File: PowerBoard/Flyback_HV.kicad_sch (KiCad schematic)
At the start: 62 parts, among them Q2 FDD86250-F085, Q3 FGH50T65SQD-F155, Q5 TN2130K1-G, Q6 STD11N60DM2, Q7 FGH50T65SQD-F155, T1 750032050, U2 LT3750, U4 MCP14A0454-E/SN

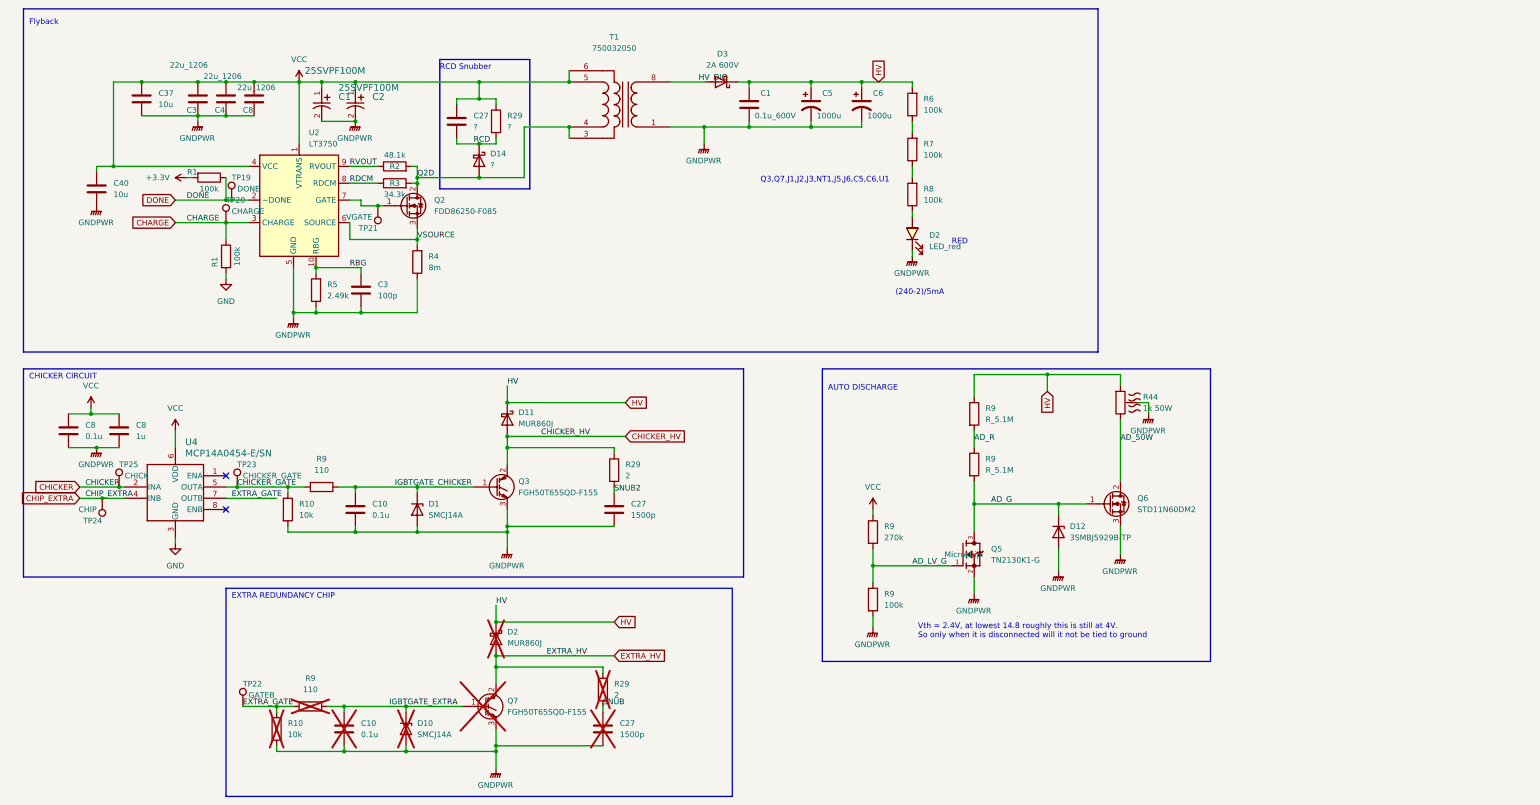
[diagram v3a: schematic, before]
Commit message: power board and midplate updates (mostly finalized)
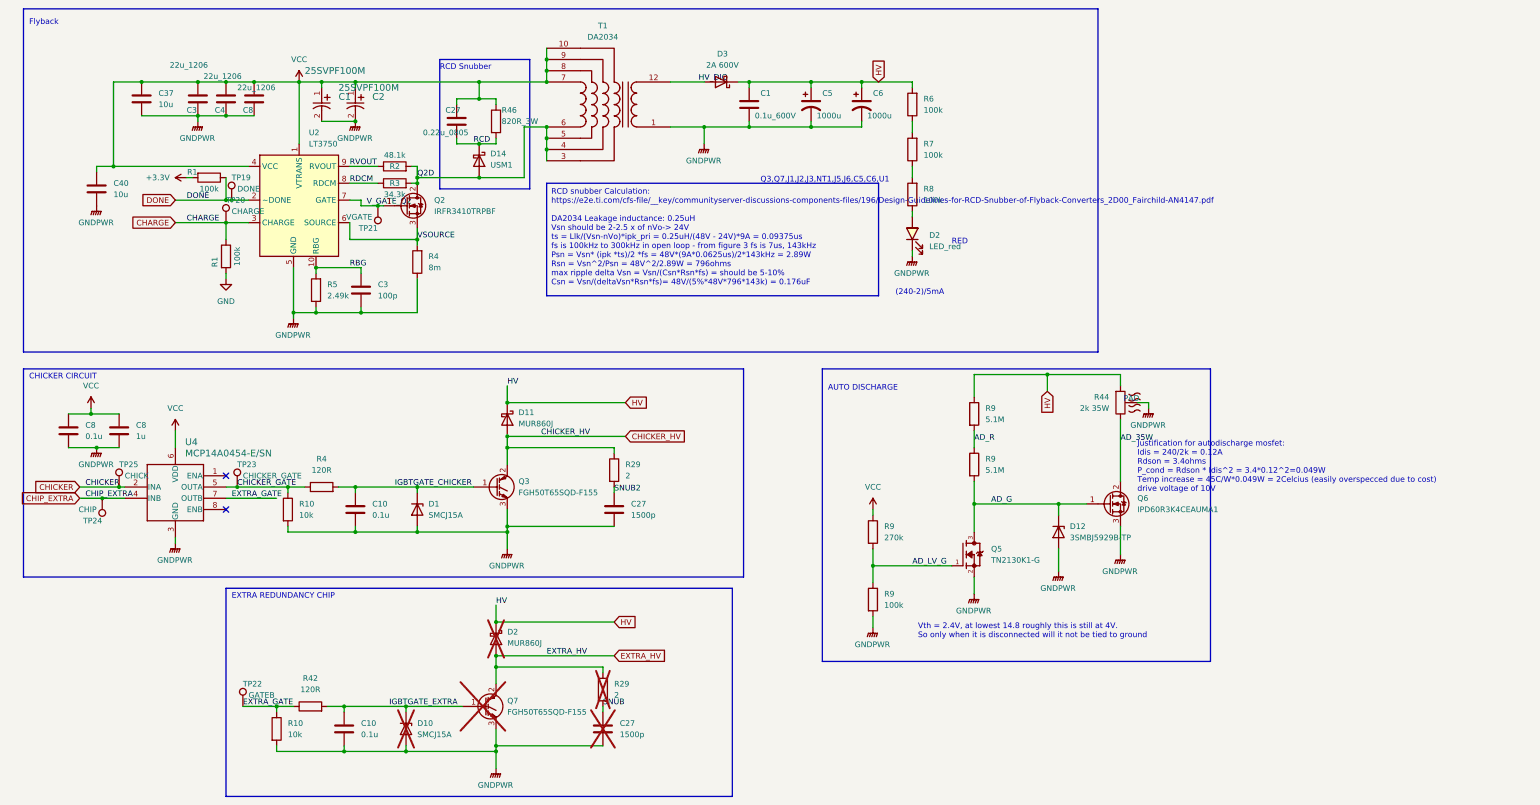
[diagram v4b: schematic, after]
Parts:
- removed C27: ?, bots:C_0805_2012Metric, symbol bots:C_1500p
- removed D1, D10: SMCJ14A, bots:D_SMC, symbol bots:SMCJ14A
- removed D14: ?, bots:D_SMA, symbol bots:MURS160-E3/52T
- removed Q2: FDD86250-F085, bots:DPAK-3_ONS, symbol bots:FDD86250-F085
- removed Q6: STD11N60DM2, bots:DPAK-3_ONS, symbol bots:STD11N60DM2
- removed R29: ?, bots:R_0805_2012Metric, symbol bots:R_2R_0805
- removed R44: 1k 50W, bots:TO-263-2, symbol bots:1k 50W
- removed R9 (x2): 110, bots:R_0603_1608Metric, symbol bots:R_110R
- removed T1: 750032050, bots:SMT_32050_WRE, symbol bots:Wurth_750032050
- added C27: 0.22u_0805, bots:C_0805_2012Metric, symbol bots:C_0.22u_0805
- added D1, D10: SMCJ15A, bots:D_SMC, symbol bots:SMCJ15A
- added D14: USM1, bots:D_SMA, symbol bots:D_USM1
- added Q2: IRFR3410TRPBF, bots:DPAK-3_ONS, symbol bots:IRFR3410TRPBF
- added Q6: IPD60R3K4CEAUMA1, bots:DPAK-3_ONS, symbol bots:IPD60R3K4CEAUMA1
- added R4, R42: 120R, bots:R_0603_1608Metric, symbol bots:R_120R
- added R44: 2k 35W, bots:TO-220-2_Horizontal_TabDown, symbol bots:2k_35W
- added R46: 820R_3W, bots:R_2512_6332Metric, symbol bots:R_820R_3W
- added T1: DA2034, bots:DA2034-ALD_COC, symbol bots:DA2034
- C10: now fitted; now in the parts list
- C27, D2, Q7, R29: now left out of the parts list
- D12: LCSC (none) -> N/A
- D2: footprint bots:LED_1206_3216Metric -> bots:LED_1206MERGE0805; JLC SMD,1.5x3.2mm -> 0805; JLC Extended (none) -> no; LCSC C2908310 -> C84256; MPN RF-RUT112TS-BD -> NCD0805R1; Manufacturer Refond -> Foshan NationStar Optoelectronics; Price 0.1023 -> 0.0122
- Q5: JLC Extended (none) -> yes; MF (none) -> Diodes Inc.; Price 0.67 -> 0.65
- R10: JLC Extended (none) -> no; now fitted; now in the parts list
- R10, R9: JLC Extended (none) -> no
- R9: value R_5.1M -> 5.1M; JLC Extended yes -> no; LCSC C322178 -> C13320; MPN RS-03L5104FT -> 0603WAF5104T5E; Manufacturer FH (Guangdong Fenghua Advanced Tech) -> UNI-ROYAL(Uniroyal Elec)
- R9: value R_5.1M -> 5.1M; JLC Extended (none) -> no; LCSC C322178 -> C13320; MPN RS-03L5104FT -> 0603WAF5104T5E; Manufacturer FH (Guangdong Fenghua Advanced Tech) -> UNI-ROYAL(Uniroyal Elec)
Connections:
- net AD_G: now also Q6.1 (G)
- net CHICKER_GATE: now also R4.1
- net EXTRA_GATE: now also R42.1
- net GND: no longer U4.3 (GND)
- net GNDPWR: now also U4.3 (GND), D1.2 (A), D10.2 (A), Q6.3 (S), R44.3 (PAD), T1.1 (SB)
- net HV: now also R44.1
- net HV_DIO: now also T1.12 (SB)
- net IGBTGATE_CHICKER: now also D1.1 (K), R4.2
- net IGBTGATE_EXTRA: now also D10.1 (K), R42.2
- net Q2D: now also D14.2 (A), Q2.2 (D), T1.3 (AB), T1.4 (AB), T1.5 (AB), T1.6 (AA)
- net RCD: now also C27.2, D14.1 (K), R46.2
- net VCC: now also C27.1, R46.1, T1.10 (AA), T1.7 (AA), T1.8 (AA), T1.9 (AA)
- net VSOURCE: now also Q2.3 (S)
- net V_GATE_Q2: now reaches TP21.1, U2.7 (GATE)
- net V_GATE_Q2: now also Q2.1 (G)
- new net AD_35W: Q6.2 (D), R44.2
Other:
- note added: "Justification for autodischarge mosfet: Idis = 240/2k = 0.12A Rdson = 3.4ohms P_cond = Rdson * Idis^2 = 3.4*0.12^2=0.049W Temp increase = 45C/W*0.049W = 2Celcius (easily overspecced due to cost) drive voltage of 10V"

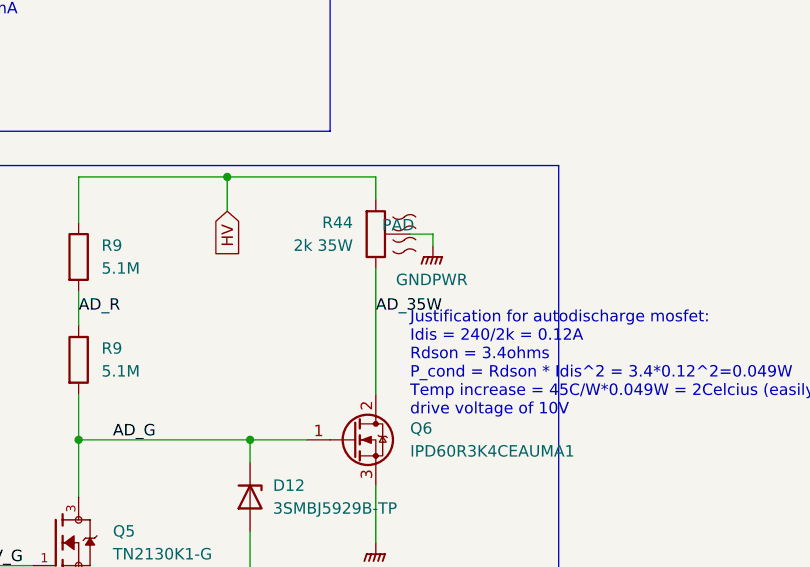
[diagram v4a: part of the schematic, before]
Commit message: discharge circuit changes
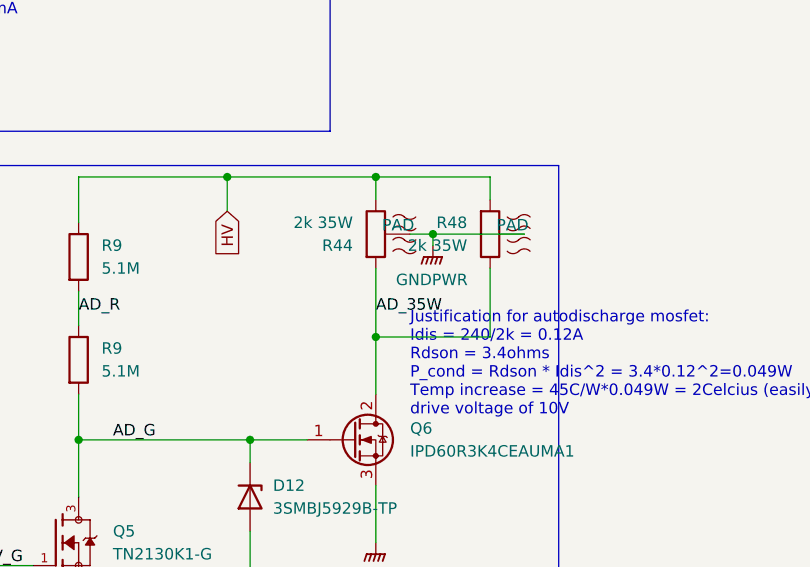
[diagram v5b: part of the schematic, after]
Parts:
- added R48: 2k 35W, bots:TO-220-2_Horizontal_TabDown, symbol bots:2k_35W
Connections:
- net AD_35W: now also R44.1, R48.2; no longer R44.2
- net GNDPWR: now also R48.3 (PAD)
- net HV: now also R44.2, R48.1; no longer R44.1
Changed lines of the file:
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@@
   (junction (at 104.14 53.34) (diameter 0) (color 0 0 0 0)
   )
+  (junction (at 262.89 97.79) (diameter 0) (color 0 0 0 0)
+  )
+  (junction (at 262.89 115.57) (diameter 0) (color 0 0 0 0)
+  )
   (junction (at 60.96 39.37) (diameter 0) (color 0 0 0 0)
   )
@@
   (junction (at 118.11 53.34) (diameter 0) (color 0 0 0 0)
   )
+  (junction (at 269.24 104.14) (diameter 0) (color 0 0 0 0)
+  )
   (junction (at 91.44 83.82) (diameter 0) (color 0 0 0 0)
   )
@@
     (stroke (width 0) (type default))
   )
+  (wire (pts (xy 275.59 115.57) (xy 262.89 115.57))
+    (stroke (width 0) (type default))
+  )
   (wire (pts (xy 113.03 35.56) (xy 118.11 35.56))
     (stroke (width 0) (type default))
@@
     (stroke (width 0) (type default))
   )
+  (wire (pts (xy 275.59 97.79) (xy 262.89 97.79))
+    (stroke (width 0) (type default))
+  )
   (wire (pts (xy 121.92 149.86) (xy 121.92 153.67))
     (stroke (width 0) (type default))
@@
     (stroke (width 0) (type default))
   )
+  (wire (pts (xy 275.59 107.95) (xy 275.59 115.57))
+    (stroke (width 0) (type default))
+  )
   (wire (pts (xy 113.03 36.83) (xy 113.03 35.56))
     (stroke (width 0) (type default))
@@
     (stroke (width 0) (type default))
   )
+  (wire (pts (xy 275.59 100.33) (xy 275.59 97.79))
+    (stroke (width 0) (type default))
+  )
   (wire (pts (xy 91.44 59.69) (xy 91.44 58.42))
     (stroke (width 0) (type default))
@@
     (stroke (width 0) (type default))
   )
+  (wire (pts (xy 269.24 104.14) (xy 279.4 104.14))
+    (stroke (width 0) (type default))
+  )
   (wire (pts (xy 179.07 31.75) (xy 193.04 31.75))
     (stroke (width 0) (type default))
@@
     (stroke (width 0) (type default))
   )
-  (wire (pts (xy 262.89 107.95) (xy 262.89 121.92))
+  (wire (pts (xy 262.89 107.95) (xy 262.89 115.57))
     (stroke (width 0) (type default))
   )
@@
     (stroke (width 0) (type default))
   )
+  (wire (pts (xy 262.89 115.57) (xy 262.89 121.92))
+    (stroke (width 0) (type default))
+  )
   (wire (pts (xy 25.4 106.68) (xy 30.48 106.68))
     (stroke (width 0) (type default))
@@
     )
   )
-  (symbol (lib_id "bots:2k_35W") (at 262.89 104.14 0) (unit 1)
-    (in_bom yes) (on_board yes) (dnp no) (fields_autoplaced)
-    (property "Reference" "R44" (at 260.35 102.87 0)
-      (effects (font (size 1.27 1.27)) (justify right))
-    )
-    (property "Value" "2k 35W" (at 260.35 105.41 0)
-      (effects (font (size 1.27 1.27)) (justify right))
-    )
-    (property "Footprint" "bots:TO-220-2_Horizontal_TabDown" (at 261.112 104.14 90)
-      (effects (font (size 1.27 1.27)) hide)
-    )
-    (property "Datasheet" "~" (at 262.89 104.14 0)
-      (effects (font (size 1.27 1.27)) hide)
-    )
-    (property "MPN" "PWR220T-35-2001J" (at 262.89 104.14 0)
-      (effects (font (size 1.27 1.27)) hide)
-    )
-    (property "Manufacturer" "Bourns" (at 262.89 104.14 0)
-      (effects (font (size 1.27 1.27)) hide)
-    )
-    (property "Price" "4.067" (at 262.89 104.14 0)
-      (effects (font (size 1.27 1.27)) hide)
-    )
-    (property "JLC" "" (at 262.89 104.14 0)
-      (effects (font (size 1.27 1.27)) hide)
-    )
-    (property "LCSC" "" (at 262.89 104.14 0)
-      (effects (font (size 1.27 1.27)) hide)
-    )
-    (pin "1")
-    (pin "2")
-    (pin "3")
-    (instances
-      (project "POWER_BOARD"
-        (path "/1a9ce3e8-a091-496c-9c5f-e7b2eb60e275/aa68550e-c35d-4fef-b4e5-f1eb6225215f"
-          (reference "R44") (unit 1)
-        )
-      )
-    )
-  )
   (symbol (lib_id "bots:C_1000u_POL_reversed") (at 204.47 36.83 0) (unit 1)
     (in_bom yes) (on_board yes) (dnp no)
@@
     )
   )
+  (symbol (lib_id "bots:2k_35W") (at 262.89 104.14 0) (mirror x) (unit 1)
+    (in_bom yes) (on_board yes) (dnp no)
+    (property "Reference" "R44" (at 260.35 105.41 0)
+      (effects (font (size 1.27 1.27)) (justify right))
+    )
+    (property "Value" "2k 35W" (at 260.35 102.87 0)
+      (effects (font (size 1.27 1.27)) (justify right))
+    )
+    (property "Footprint" "bots:TO-220-2_Horizontal_TabDown" (at 261.112 104.14 90)
+      (effects (font (size 1.27 1.27)) hide)
+    )
+    (property "Datasheet" "~" (at 262.89 104.14 0)
+      (effects (font (size 1.27 1.27)) hide)
+    )
+    (property "MPN" "PWR220T-35-2001J" (at 262.89 104.14 0)
+      (effects (font (size 1.27 1.27)) hide)
+    )
+    (property "Manufacturer" "Bourns" (at 262.89 104.14 0)
+      (effects (font (size 1.27 1.27)) hide)
+    )
+    (property "Price" "4.067" (at 262.89 104.14 0)
+      (effects (font (size 1.27 1.27)) hide)
+    )
+    (property "JLC" "" (at 262.89 104.14 0)
+      (effects (font (size 1.27 1.27)) hide)
+    )
+    (property "LCSC" "" (at 262.89 104.14 0)
+      (effects (font (size 1.27 1.27)) hide)
+    )
+    (pin "1")
+    (pin "2")
+    (pin "3")
+    (instances
+      (project "POWER_BOARD"
+        (path "/1a9ce3e8-a091-496c-9c5f-e7b2eb60e275/aa68550e-c35d-4fef-b4e5-f1eb6225215f"
+          (reference "R44") (unit 1)
+        )
+      )
+    )
+  )
   (symbol (lib_id "bots:R_34k") (at 99.06 54.61 90) (unit 1)
     (in_bom yes) (on_board yes) (dnp no)
@@
         )
       )
+    )
+  )
+  (symbol (lib_id "bots:2k_35W") (at 275.59 104.14 0) (unit 1)
+    (in_bom yes) (on_board yes) (dnp no) (fields_autoplaced)
+    (property "Reference" "R48" (at 273.05 102.87 0)
+      (effects (font (size 1.27 1.27)) (justify right))
+    )
+    (property "Value" "2k 35W" (at 273.05 105.41 0)
+      (effects (font (size 1.27 1.27)) (justify right))
+    )
+    (property "Footprint" "bots:TO-220-2_Horizontal_TabDown" (at 273.812 104.14 90)
+      (effects (font (size 1.27 1.27)) hide)
+    )
+    (property "Datasheet" "~" (at 275.59 104.14 0)
+      (effects (font (size 1.27 1.27)) hide)
+    )
+    (property "MPN" "PWR220T-35-2001J" (at 275.59 104.14 0)
+      (effects (font (size 1.27 1.27)) hide)
+    )
+    (property "Manufacturer" "Bourns" (at 275.59 104.14 0)
+      (effects (font (size 1.27 1.27)) hide)
+    )
+    (property "Price" "4.067" (at 275.59 104.14 0)
+      (effects (font (size 1.27 1.27)) hide)
+    )
+    (property "JLC" "" (at 275.59 104.14 0)
+      (effects (font (size 1.27 1.27)) hide)
+    )
+    (property "LCSC" "" (at 275.59 104.14 0)
+      (effects (font (size 1.27 1.27)) hide)
+    )
+    (pin "1")
+    (pin "2")
+    (pin "3")
+    (instances
+      (project "POWER_BOARD"
+        (path "/1a9ce3e8-a091-496c-9c5f-e7b2eb60e275/aa68550e-c35d-4fef-b4e5-f1eb6225215f"
+          (reference "R48") (unit 1)
+        )
+      )
